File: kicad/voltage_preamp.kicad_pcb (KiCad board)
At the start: 4 copper layers, 104.1 x 68.6 mm, 34 parts, among them J1 Conn_Coaxial, J2 Conn_01x01_Male, J3 Conn_01x01_Male, J4 Conn_01x01_Male, J5 Conn_Coaxial, J6 Conn_01x02_Male, U1 lmp7721, U2 lmp7721, U3 lmp7721, U4 OPA211, U6 OPA211

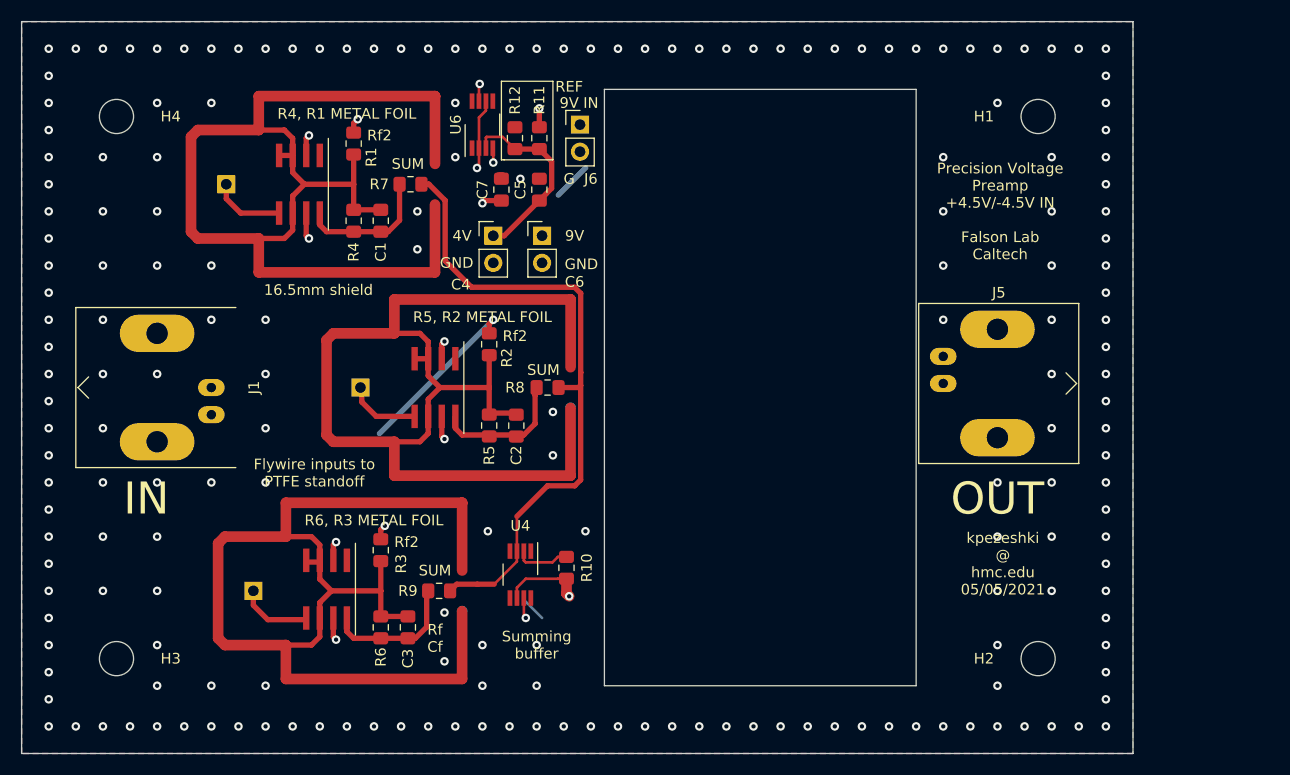
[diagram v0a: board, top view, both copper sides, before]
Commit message: now using 4.5V of AAA cells for power, power input available, SMAs for power input and output
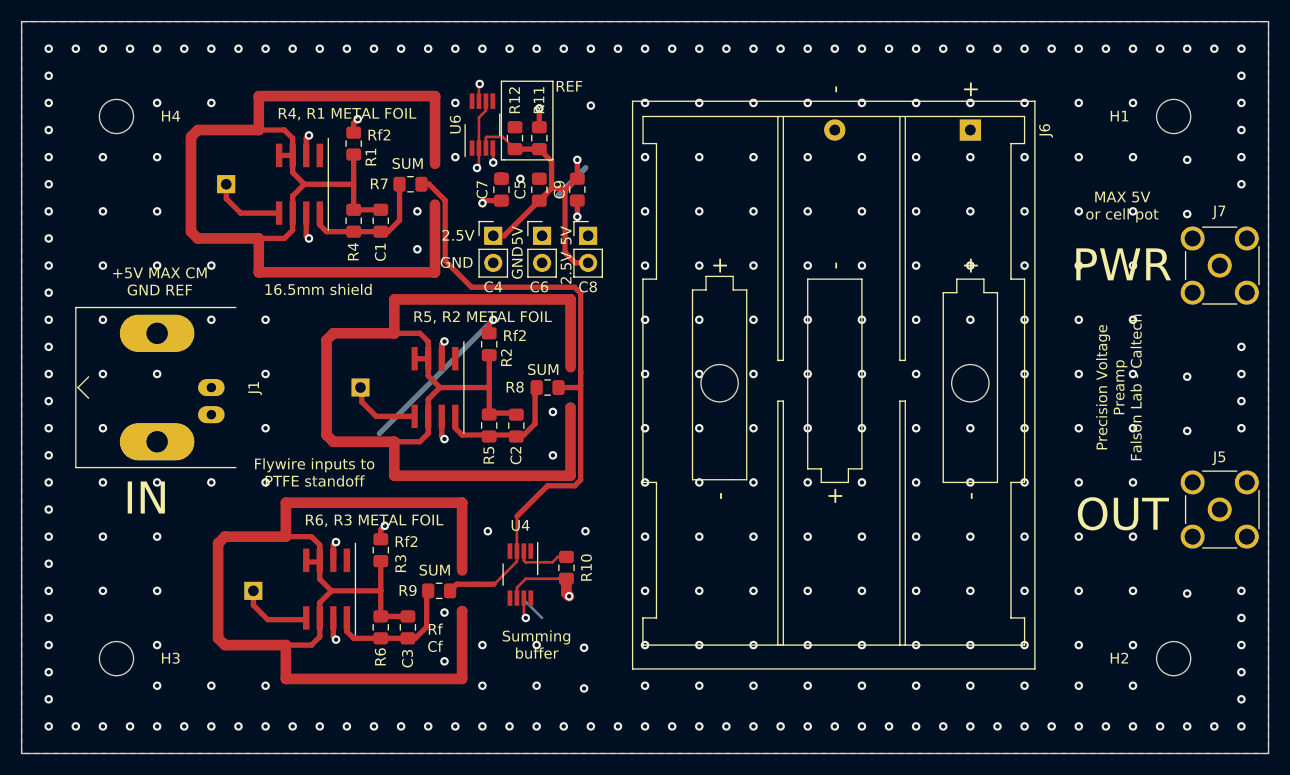
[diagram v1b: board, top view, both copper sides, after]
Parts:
- added C8: CP, Connector_PinHeader_2.54mm:PinHeader_1x02_P2.54mm_Vertical, F.Cu at (162.3, 129.3)
- added C9: C, Capacitor_SMD:C_0805_2012Metric_Pad1.15x1.40mm_HandSolder, F.Cu at (161.3, 125.0)
- added J7: Conn_01x02_Male, Connector_Coaxial:SMA_Molex_73251-2200_Horizontal, F.Cu at (221.5, 132.1)
- J5: footprint Connector_Coaxial:BNC_Amphenol_B6252HB-NPP3G-50_Horizontal -> Connector_Coaxial:SMA_Molex_73251-2200_Horizontal
- J6: footprint Connector_PinHeader_2.54mm:PinHeader_1x02_P2.54mm_Vertical -> Battery:BatteryHolder_Keystone_2479_3xAAA
- moved J6 36.6 mm to (198.1, 119.4), turned to 270 degrees
- moved J5 28.5 mm to (221.5, 154.9)
- moved H1 12.7 mm to (217.2, 118.1)
- moved H2 12.7 mm to (217.2, 168.9)
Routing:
- net +4V: track 101.3 -> 119.4 mm
- net Net-(J5-Pad1): track 77.8 -> 93.3 mm
- net /4VRES: track 18.0 -> 31.0 mm, vias 0 -> 1
- net +9V: track 13.2 -> 14.3 mm, vias 7 -> 8
- net GND: vias 195 -> 175
- net (no net): vias 0 -> 129
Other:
- board size 104.1 x 68.6 mm -> 116.8 x 68.6 mm
- board text added: "+5V MAX CM GND REF"
- board text added: "2.5V"
- board text added: "5V"
- board text added: "MAX 5V or cell pot"
- board text added: "PWR"
- board text added: "Precision Voltage Preamp Falson Lab - Caltech"
- board text removed: "4V"
- board text removed: "9V"
- board text removed: "G"
- board text removed: "Precision Voltage Preamp +4.5V/-4.5V IN Falson Lab Caltech"
- board text removed: "kpezeshki @ hmc.edu 05/05/2021"

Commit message: fixed via shielding, now using bnc as output and power connectors
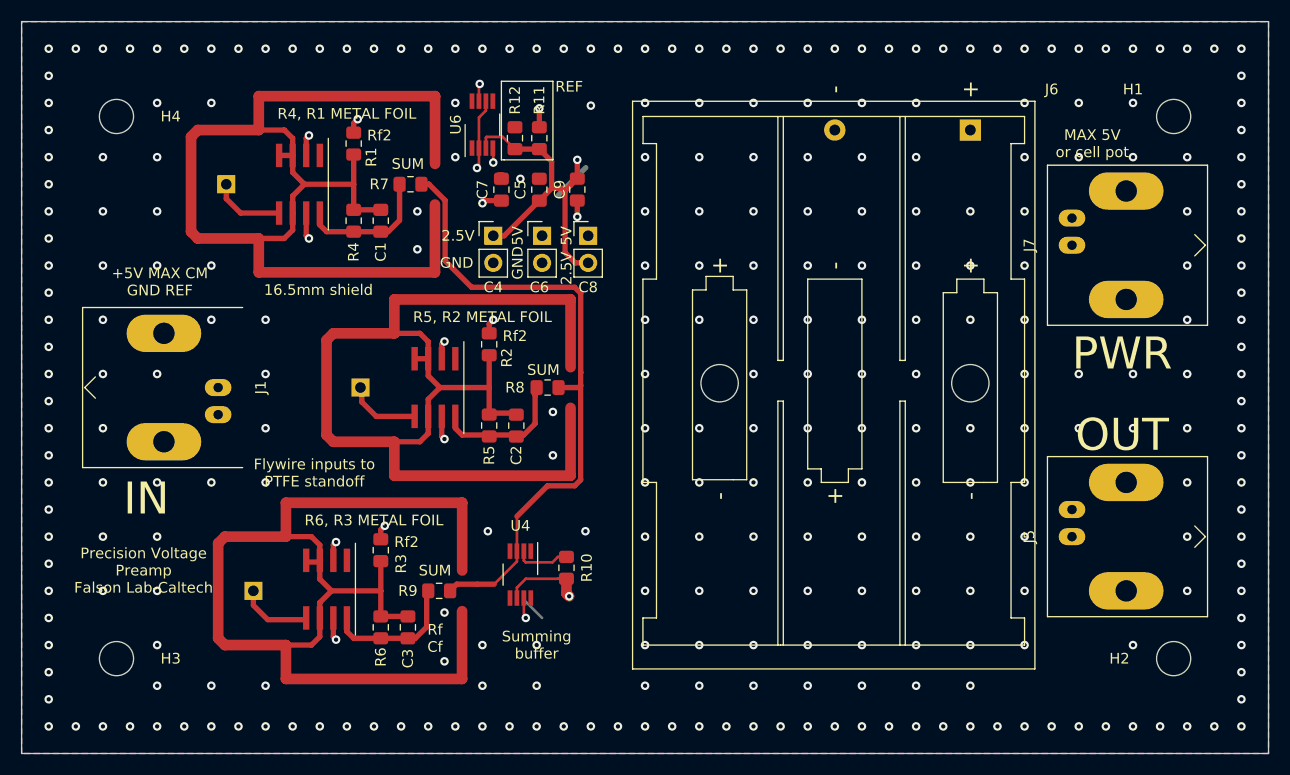
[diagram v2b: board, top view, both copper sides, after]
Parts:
- J5, J7: footprint Connector_Coaxial:SMA_Molex_73251-2200_Horizontal -> Connector_Coaxial:BNC_Amphenol_B6252HB-NPP3G-50_Horizontal
- moved J5 14.1 mm to (207.6, 157.5)
- moved J7 14.0 mm to (207.6, 130.2)
- moved J1 0.64 mm to (127.6, 143.5)
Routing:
- net +4V: track 119.4 -> 88.3 mm
- net Net-(J5-Pad1): track 93.3 -> 74.8 mm
- net (no net): track 0.01 -> 0.00 mm, vias 129 -> 15
- net GND: vias 175 -> 281
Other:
- board text added: "Precision Voltage Preamp Falson Lab-Caltech"
- board text removed: "Precision Voltage Preamp Falson Lab - Caltech"
